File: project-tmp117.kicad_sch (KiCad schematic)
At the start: 17 parts, among them J1 Conn_01x01_Pin, J2 Conn_01x01_Pin, J3 Conn_01x01_Pin, J4 Conn_01x01_Pin, J5 Conn_01x01_Pin, J7 SM04B-SRSS-TB(LF)(SN), J8 SM04B-SRSS-TB(LF)(SN), U1 TMP117AIDRVR

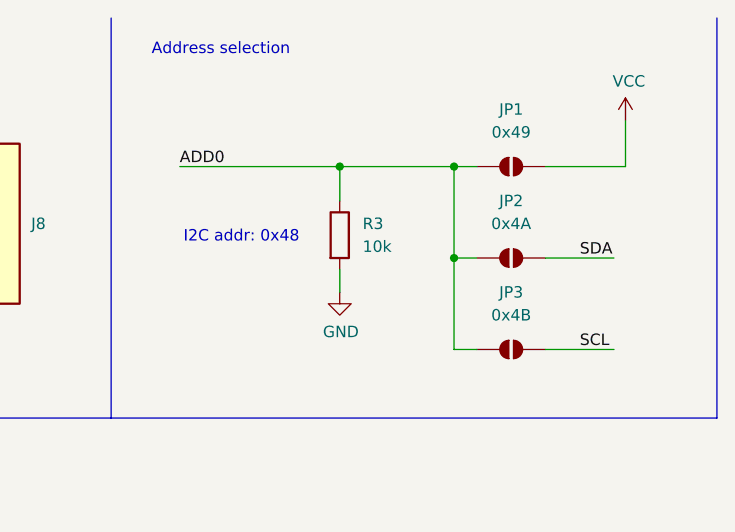
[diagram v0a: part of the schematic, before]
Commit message: Add a jumper for address 0x48
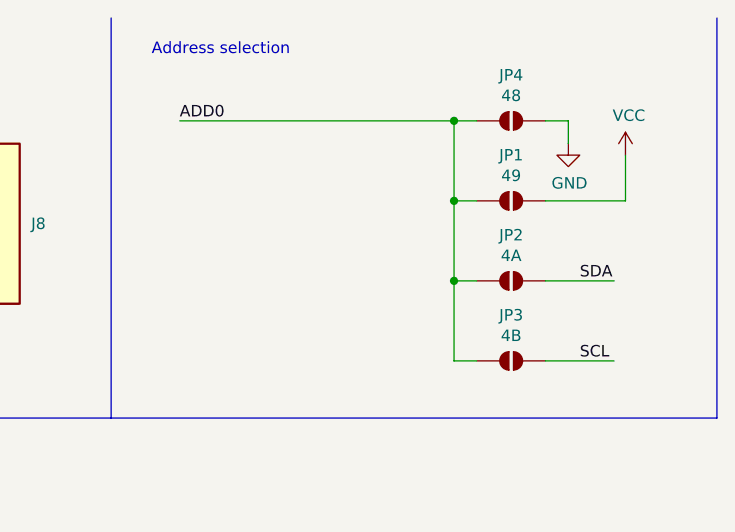
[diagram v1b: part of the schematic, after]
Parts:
- removed R3: 10k, Resistor_SMD:R_0603_1608Metric, symbol Device:R
- added JP4: 48, Jumper:SolderJumper-2_P1.3mm_Open_RoundedPad1.0x1.5mm, symbol Jumper:SolderJumper_2_Open
- JP1: value 0x49 -> 49
- JP2: value 0x4A -> 4A
- JP3: value 0x4B -> 4B
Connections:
- net ADD0: now also JP4.1 (A)
- net GND: now also JP4.2 (B)
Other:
- note removed: "I2C addr: 0x48"
- moved on the sheet: JP1, JP2, JP3

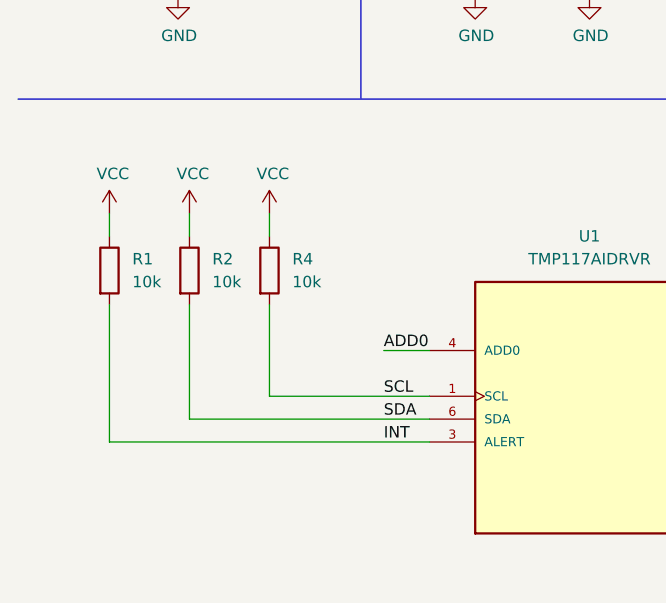
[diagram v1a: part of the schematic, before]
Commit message: Remove the ALERT pull-up
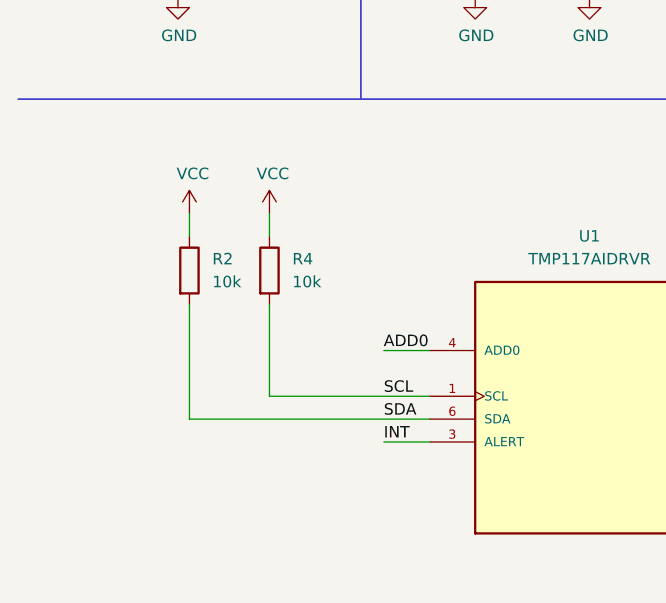
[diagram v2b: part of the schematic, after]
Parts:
- removed R1: 10k, Resistor_SMD:R_0603_1608Metric, symbol Device:R
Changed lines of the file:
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@@
-	(wire
-		(pts
-			(xy 22.86 69.85) (xy 22.86 72.39)
-		)
-		(stroke
-			(width 0)
-			(type default)
-		)
-	)
 	(wire
 		(pts
@@
 	(wire
 		(pts
-			(xy 22.86 95.25) (xy 22.86 80.01)
-		)
-		(stroke
-			(width 0)
-			(type default)
-		)
-	)
-	(wire
-		(pts
 			(xy 189.23 33.02) (xy 189.23 41.91)
 		)
@@
 	(wire
 		(pts
-			(xy 58.42 95.25) (xy 22.86 95.25)
-		)
-		(stroke
-			(width 0)
-			(type default)
-		)
-	)
-	(wire
-		(pts
 			(xy 27.94 41.91) (xy 30.48 41.91)
 		)
@@
 		(pts
 			(xy 40.64 69.85) (xy 40.64 72.39)
+		)
+		(stroke
+			(width 0)
+			(type default)
+		)
+	)
+	(wire
+		(pts
+			(xy 53.34 95.25) (xy 58.42 95.25)
 		)
 		(stroke
@@
 	(symbol
 		(lib_id "power:VCC")
-		(at 22.86 69.85 0)
-		(unit 1)
-		(exclude_from_sim no)
-		(in_bom yes)
-		(on_board yes)
-		(dnp no)
-		(property "Reference" "#PWR08"
-			(at 22.86 73.66 0)
-			(effects
-				(font
-					(size 1.27 1.27)
-				)
-				(hide yes)
-			)
-		)
-		(property "Value" "VCC"
-			(at 23.241 65.4558 0)
-			(effects
-				(font
-					(size 1.27 1.27)
-				)
-			)
-		)
-		(property "Footprint" ""
-			(at 22.86 69.85 0)
-			(effects
-				(font
-					(size 1.27 1.27)
-				)
-				(hide yes)
-			)
-		)
-		(property "Datasheet" ""
-			(at 22.86 69.85 0)
-			(effects
-				(font
-					(size 1.27 1.27)
-				)
-				(hide yes)
-			)
-		)
-		(property "Description" ""
-			(at 22.86 69.85 0)
-			(effects
-				(font
-					(size 1.27 1.27)
-				)
-				(hide yes)
-			)
-		)
-		(pin "1"
-		)
-		(instances
-			(project "project-tmp117"
-				(path "/98c9e280-7660-4ce7-b6c8-d4c1f6cd8632"
-					(reference "#PWR08")
-					(unit 1)
-				)
-			)
-		)
-	)
-	(symbol
-		(lib_id "power:VCC")
 		(at 76.2 27.94 0)
 		(unit 1)
@@
 					(unit 1)
 				)
-			)
-		)
-	)
-	(symbol
-		(lib_id "Device:R")
-		(at 22.86 76.2 0)
-		(unit 1)
-		(exclude_from_sim no)
-		(in_bom yes)
-		(on_board yes)
-		(dnp no)
-		(fields_autoplaced yes)
-		(property "Reference" "R1"
-			(at 25.4 74.9299 0)
-			(effects
-				(font
-					(size 1.27 1.27)
-				)
-				(justify left)
-			)
-		)
-		(property "Value" "10k"
-			(at 25.4 77.4699 0)
-			(effects
-				(font
-					(size 1.27 1.27)
-				)
-				(justify left)
-			)
-		)
-		(property "Footprint" "Resistor_SMD:R_0603_1608Metric"
-			(at 21.082 76.2 90)
-			(effects
-				(font
-					(size 1.27 1.27)
-				)
-				(hide yes)
-			)
-		)
-		(property "Datasheet" "~"
-			(at 22.86 76.2 0)
-			(effects
-				(font
-					(size 1.27 1.27)
-				)
-				(hide yes)
-			)
-		)
-		(property "Description" "Resistor"
-			(at 22.86 76.2 0)
-			(effects
-				(font
-					(size 1.27 1.27)
-				)
-				(hide yes)
-			)
-		)
-		(pin "2"
-		)
-		(pin "1"
-		)
-		(instances
-			(project "project-tmp117"
-				(path "/98c9e280-7660-4ce7-b6c8-d4c1f6cd8632"
-					(reference "R1")
-					(unit 1)
-				)
